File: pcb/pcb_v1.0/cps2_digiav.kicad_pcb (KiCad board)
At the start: 2 copper layers, 93.6 x 46.2 mm, 134 parts, among them J4 HDMI_CONN, P1 JTAG_CONN, U10 S25FL116K, U12 TLV70012, U13 TLV70025, U14 TLV70012, U15 TLV70018, U16 TLV70018, U2 EP4CE15E22, U3 IT6613, U31 74LVC245, U32 74LVC245, U33 74LVC245, U34 SN74LVC3G17, U7 TC1262-3.3VDBTR, U8 TLV70033

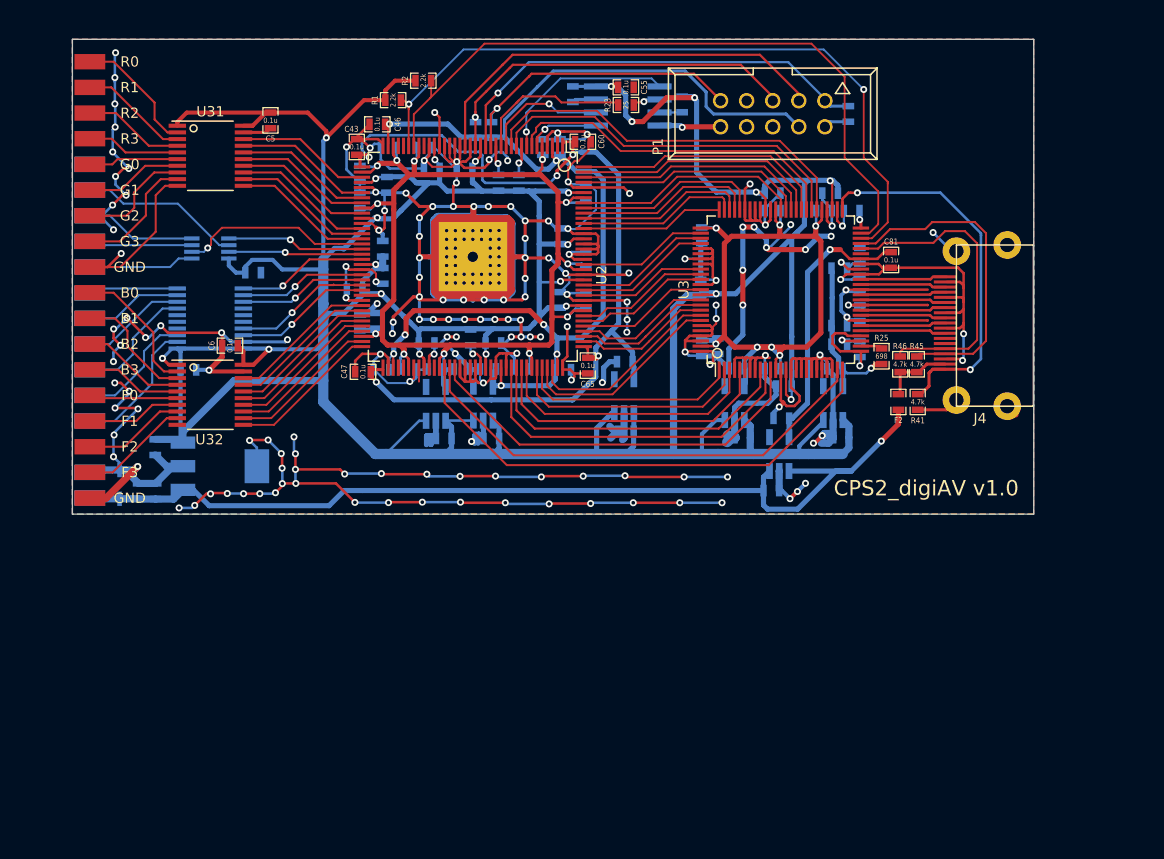
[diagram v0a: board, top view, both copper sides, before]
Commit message: Moved ICs to top, made to fit ontop of CPS2 DIPs
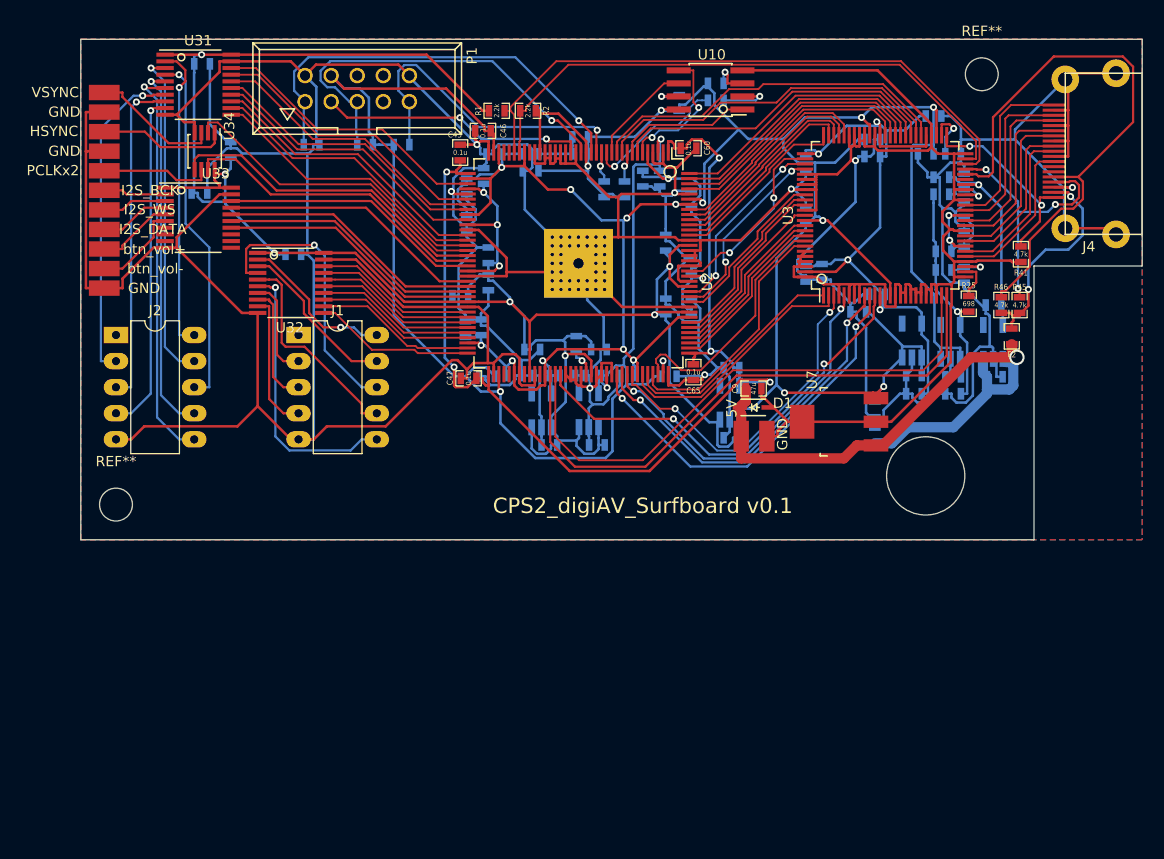
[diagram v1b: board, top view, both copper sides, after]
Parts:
- removed W10: G3, custom_components:SMD_PAD
- removed W11: B0, custom_components:SMD_PAD
- removed W12: B1, custom_components:SMD_PAD
- removed W13: B2, custom_components:SMD_PAD
- removed W14: B3, custom_components:SMD_PAD
- removed W15: F0, custom_components:SMD_PAD
- removed W16: F1, custom_components:SMD_PAD
- removed W17: F2, custom_components:SMD_PAD
- removed W18: F3, custom_components:SMD_PAD
- removed W27, W28: GND, custom_components:SMD_PAD
- removed W3: R0, custom_components:SMD_PAD
- removed W4: R1, custom_components:SMD_PAD
- removed W5: R2, custom_components:SMD_PAD
- removed W6: R3, custom_components:SMD_PAD
- removed W7: G0, custom_components:SMD_PAD
- removed W8: G1, custom_components:SMD_PAD
- removed W9: G2, custom_components:SMD_PAD
- added J1: Conn_02x05, Housings_DIP:DIP-10_W7.62mm_LongPads, F.Cu at (60.3, 52.3)
- added J2: Conn_02x05, Housings_DIP:DIP-10_W7.62mm_LongPads, F.Cu at (42.5, 52.3)
- added REF**: MountingHole_3.2mm_M3, Mounting_Holes:MountingHole_3.2mm_M3, F.Cu at (126.9, 26.9)
- added REF**: MountingHole_3.2mm_M3, Mounting_Holes:MountingHole_3.2mm_M3, F.Cu at (42.5, 68.8)
- C5, C55, C6, C81, R23: moved to B.Cu
- C9, D1, U10, U33, U34, U7, W1, W19, W2, W20, W21, W22, W23, W24, W25, W26, W29, W30, W31: moved to F.Cu
- moved C1 70.3 mm to (116.5, 62.1)
- moved C3 70.2 mm to (116.5, 59.6)
- moved W31 66.0 mm to (105.9, 62.2), turned to 90 degrees
- moved W1 63.7 mm to (103.4, 62.2), turned to 90 degrees
- moved D1 62.3 mm to (104.7, 59.4), turned to 0 degrees
- moved C9 60.7 mm to (104.6, 57.5), turned to 0 degrees
- moved U7 60.5 mm to (113.0, 60.8)
- moved R20 52.4 mm to (61.6, 33.8), turned to 180 degrees
- moved P1 40.5 mm to (66.0, 28.3), turned to 0 degrees
- moved C2 24.4 mm to (128.1, 56.4)
- moved U8 23.5 mm to (128.0, 53.0)
- moved C4 23.4 mm to (128.0, 49.4)
- moved J4 19.8 mm to (135.0, 34.7)
- moved U15 18.3 mm to (120.1, 52.9)
- moved C87 17.8 mm to (120.3, 56.3)
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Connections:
- U33 pad 11: /fpga1/I2S_BCK -> Net-(U33-Pad11)
- U33 pad 12: /fpga1/I2S_WS -> Net-(U33-Pad12)
- U33 pad 13: /fpga1/I2S_DATA -> Net-(U33-Pad13)
- U33 pad 14: Net-(U33-Pad14) -> /fpga1/btn_vol-
- U33 pad 15: Net-(U33-Pad15) -> /fpga1/btn_vol+
- U33 pad 16: Net-(U33-Pad16) -> /fpga1/I2S_DATA
- U33 pad 17: /fpga1/btn_vol+ -> /fpga1/I2S_WS
- U33 pad 18: /fpga1/btn_vol- -> /fpga1/I2S_BCK
- W19 pad 1: Net-(U33-Pad3) -> Net-(U33-Pad5)
- W20 pad 1: Net-(U33-Pad9) -> Net-(U33-Pad2)
- W22 pad 1: Net-(U33-Pad8) -> Net-(U33-Pad3)
- W23 pad 1: Net-(U33-Pad2) -> Net-(U33-Pad6)
- W25 pad 1: Net-(U33-Pad7) -> Net-(U33-Pad4)
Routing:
- net GND: track 885.6 -> 850.0 mm, vias 171 -> 8
- net /5V: track 95.5 -> 62.9 mm
- net Net-(J2-Pad6): track 8.73 -> 39.3 mm, vias 0 -> 1
- net Net-(J2-Pad7): track 9.07 -> 36.3 mm, vias 0 -> 1
- net /hdmitx1/DDC_SCL: track 30.4 -> 56.2 mm
- net /IOVDD: track 450.2 -> 425.4 mm, vias 22 -> 18
- net Net-(J2-Pad8): track 9.84 -> 34.5 mm, vias 0 -> 1
- net Net-(J2-Pad2): track 9.50 -> 31.8 mm, vias 0 -> 1
- net Net-(J2-Pad9): track 10.6 -> 32.5 mm, vias 0 -> 1
- net Net-(J2-Pad3): track 11.1 -> 32.3 mm, vias 0 -> 1
- net Net-(J2-Pad4): track 12.3 -> 33.2 mm, vias 0 -> 1
- net Net-(J1-Pad6): track 8.62 -> 27.2 mm, vias 0 -> 1
- net /fpga1/VSYNC_in: track 13.4 -> 31.8 mm, vias 1 -> 0
- net Net-(J2-Pad10): track 12.3 -> 29.9 mm, vias 0 -> 1
- net /fpga1/HSYNC_in: track 13.1 -> 30.4 mm, vias 1 -> 0
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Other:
- board size 93.6 x 46.2 mm -> 103.4 x 48.7 mm
- board text added: "CPS2_digiAV_Surfboard v0.1"
- board text removed: "CPS2_digiAV v1.0"

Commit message: Added ADV7513
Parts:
- added U1: ADV7513, Housings_QFP:LQFP-64_10x10mm_Pitch0.5mm, F.Cu at (90.8, 82.3)
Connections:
- J4 pad 1: /hdmitx1/TMDS_D2+ -> /hdmitx1/TX2+
- J4 pad 10: /hdmitx1/TMDS_CLK+ -> /hdmitx1/TXC+
- J4 pad 12: /hdmitx1/TMDS_CLK- -> /hdmitx1/TXC-
- J4 pad 15: /hdmitx1/DDC_SCL -> /hdmitx1/DDCSCL
- J4 pad 16: /hdmitx1/DDC_SDA -> /hdmitx1/DDCSDA
- J4 pad 3: /hdmitx1/TMDS_D2- -> /hdmitx1/TX2-
- J4 pad 4: /hdmitx1/TMDS_D1+ -> /hdmitx1/TX1+
- J4 pad 6: /hdmitx1/TMDS_D1- -> /hdmitx1/TX1-
- J4 pad 7: /hdmitx1/TMDS_D0+ -> /hdmitx1/TX0+
- J4 pad 9: /hdmitx1/TMDS_D0- -> /hdmitx1/TX0-
- R45 pad 2: /hdmitx1/DDC_SDA -> /hdmitx1/DDCSDA
- R46 pad 2: /hdmitx1/DDC_SCL -> /hdmitx1/DDCSCL
- U3 pad 1: /hdmitx1/DE -> Net-(U3-Pad1)
- U3 pad 10: /fpga1/HDMITX_I2S_WS -> Net-(U3-Pad10)
- U3 pad 11: /fpga1/HDMITX_I2S_BCK -> Net-(U3-Pad11)
- U3 pad 2: /fpga1/HDMITX_HSYNC -> Net-(U3-Pad2)
- U3 pad 24: /fpga1/HDMITX_INT_N -> Net-(U3-Pad24)
- U3 pad 25: /fpga1/HDMITX_RESET_N -> Net-(U3-Pad25)
- U3 pad 3: /fpga1/HDMITX_VSYNC -> Net-(U3-Pad3)
- U3 pad 48: /fpga1/SCL -> Net-(U3-Pad48)
- U3 pad 49: /fpga1/SDA -> Net-(U3-Pad49)
- U3 pad 5: /fpga1/AUD_MCLK -> Net-(U3-Pad5)
- U3 pad 56: /fpga1/HDMITX_R7 -> Net-(U3-Pad56)
- U3 pad 57: /fpga1/HDMITX_R6 -> Net-(U3-Pad57)
- U3 pad 58: /fpga1/HDMITX_R5 -> Net-(U3-Pad58)
- U3 pad 59: /fpga1/HDMITX_R4 -> Net-(U3-Pad59)
- U3 pad 60: /fpga1/HDMITX_R3 -> Net-(U3-Pad60)
- U3 pad 61: /fpga1/HDMITX_R2 -> Net-(U3-Pad61)
- U3 pad 62: /fpga1/HDMITX_R1 -> Net-(U3-Pad62)
- U3 pad 63: /fpga1/HDMITX_R0 -> Net-(U3-Pad63)
- U3 pad 71: /hdmitx1/G7 -> Net-(U3-Pad71)
- U3 pad 72: /hdmitx1/G6 -> Net-(U3-Pad72)
- U3 pad 73: /hdmitx1/G5 -> Net-(U3-Pad73)
- U3 pad 74: /hdmitx1/G4 -> Net-(U3-Pad74)
- U3 pad 75: /hdmitx1/G3 -> Net-(U3-Pad75)
- U3 pad 77: /hdmitx1/G2 -> Net-(U3-Pad77)
- U3 pad 78: /hdmitx1/G1 -> Net-(U3-Pad78)
- U3 pad 79: /hdmitx1/G0 -> Net-(U3-Pad79)
- U3 pad 84: /hdmitx1/B7 -> Net-(U3-Pad84)
- U3 pad 85: /hdmitx1/B6 -> Net-(U3-Pad85)
- U3 pad 86: /hdmitx1/B5 -> Net-(U3-Pad86)
- U3 pad 88: /fpga1/HDMITX_PCLK -> Net-(U3-Pad88)
- U3 pad 9: /fpga1/HDMITX_I2S_DATA -> Net-(U3-Pad9)
- U3 pad 90: /hdmitx1/B4 -> Net-(U3-Pad90)
- U3 pad 91: /hdmitx1/B3 -> Net-(U3-Pad91)
- U3 pad 92: /hdmitx1/B2 -> Net-(U3-Pad92)
- U3 pad 93: /hdmitx1/B1 -> Net-(U3-Pad93)
- U3 pad 94: /hdmitx1/B0 -> Net-(U3-Pad94)
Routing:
- net /hdmitx1/DDC_SCL: track 56.2 -> 1.09 mm
- net /hdmitx1/DDCSCL: track 0.00 -> 55.2 mm
- net Net-(U3-Pad49): track 0.00 -> 51.8 mm
- net /fpga1/SDA: track 56.4 -> 4.66 mm
- net Net-(U3-Pad25): track 0.00 -> 50.0 mm
- net /fpga1/HDMITX_RESET_N: track 56.6 -> 6.60 mm
- net Net-(U3-Pad9): track 0.00 -> 25.3 mm, vias 0 -> 1
- net /fpga1/HDMITX_I2S_DATA: track 37.5 -> 12.2 mm, vias 2 -> 1
- net /hdmitx1/DDC_SDA: track 26.2 -> 2.04 mm, vias 3 -> 1
- net /hdmitx1/DDCSDA: track 0.00 -> 24.2 mm, vias 0 -> 2
- net Net-(U3-Pad93): track 0.00 -> 23.2 mm
- net /hdmitx1/B1: track 24.1 -> 0.92 mm
- net Net-(U3-Pad94): track 0.00 -> 22.9 mm
- net /hdmitx1/B0: track 24.6 -> 1.67 mm
- net /fpga1/HDMITX_I2S_WS: track 39.1 -> 17.5 mm, vias 2 -> 1
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
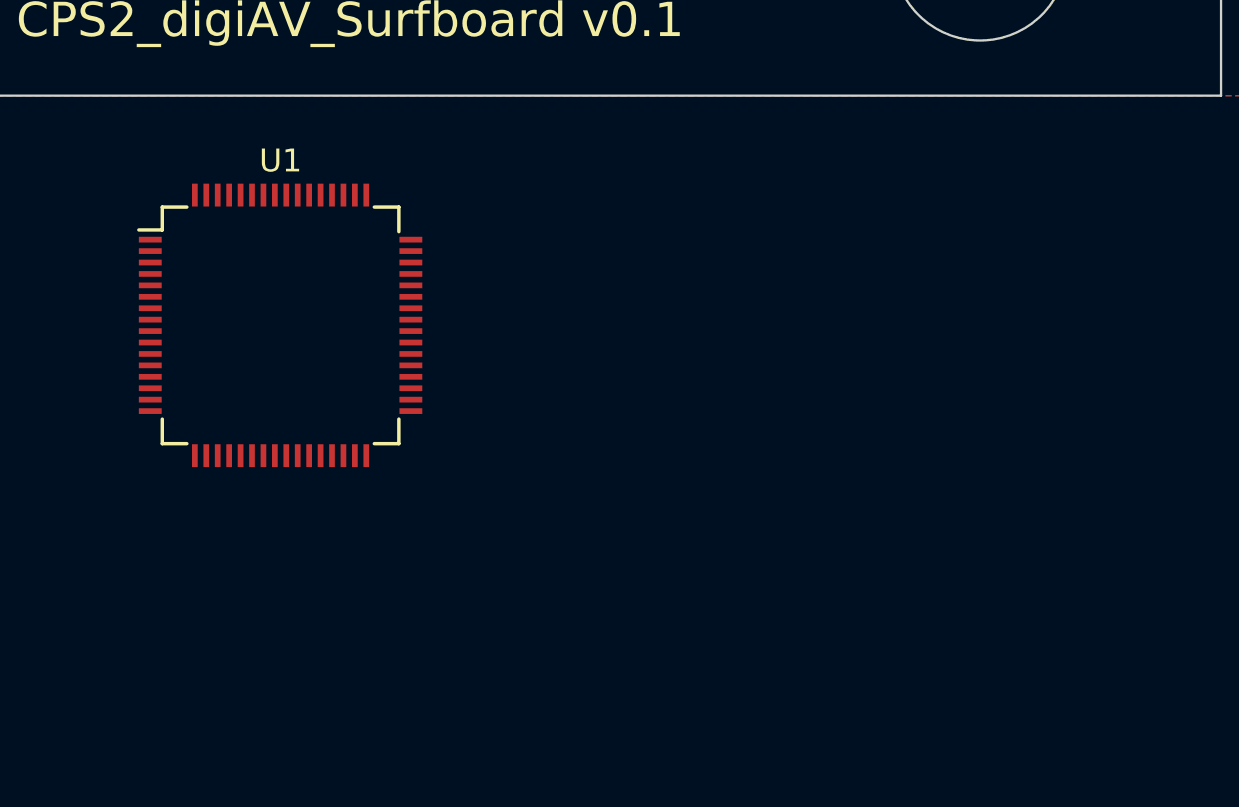
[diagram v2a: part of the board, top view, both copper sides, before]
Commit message: Finished power section of ADV7531
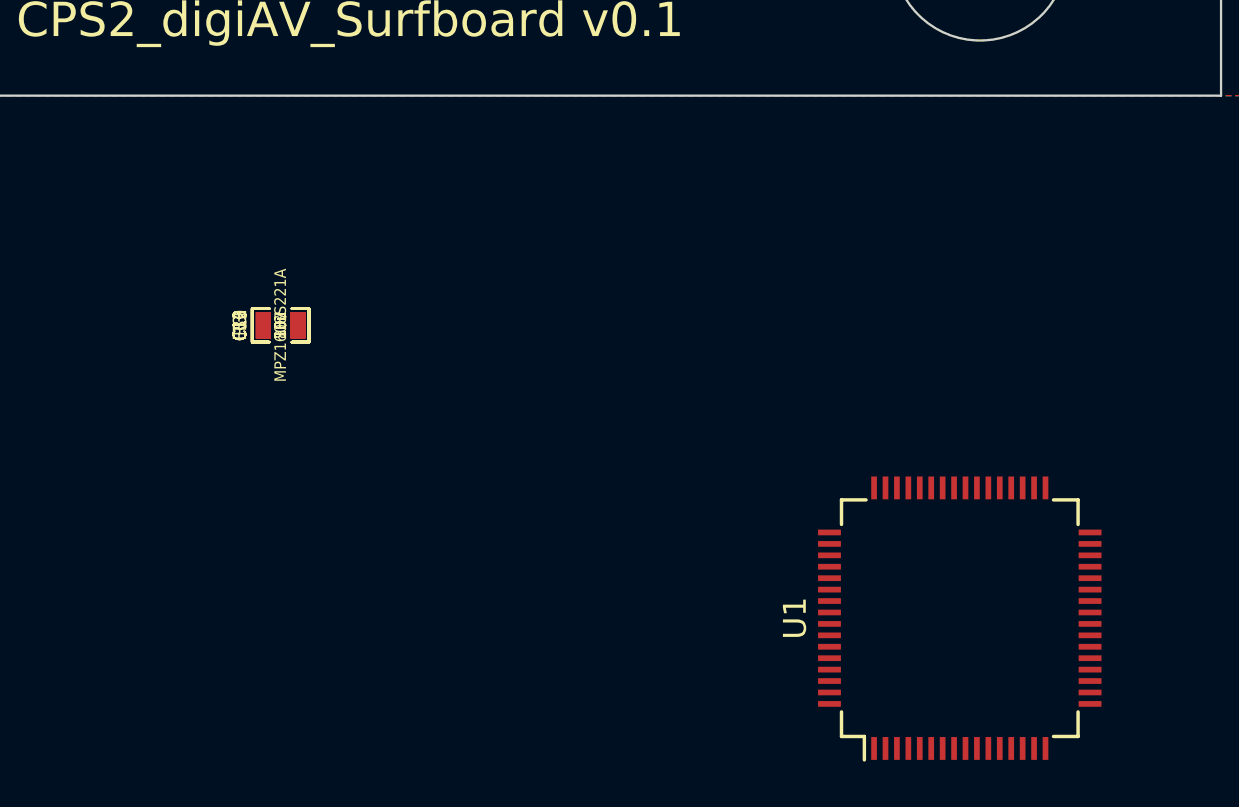
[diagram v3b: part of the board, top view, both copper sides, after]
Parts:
- added C10, C11, C12, C13: 10u, custom_components:SM0603_Capa_libcms, F.Cu at (90.8, 82.3)
- added FB3: MPZ1608S221A, custom_components:SM0603_Resistor_libcms, F.Cu at (90.8, 82.3)
- added R3: 887, custom_components:SM0603_Resistor_libcms, F.Cu at (90.8, 82.3)
- moved U1 32.4 mm to (120.5, 95.1), turned to 90 degrees
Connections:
- C110 pad 1: /hdmitx1/DVDD1V8 -> /hdmitx1/AVDD1V8
- C69 pad 1: /hdmitx1/DVDD1V8 -> Net-(C12-Pad1)
- C73 pad 1: /IOVDD -> Net-(C12-Pad1)
- C74 pad 1: Net-(C74-Pad1) -> /hdmitx1/AVDD1V8
- C75 pad 1: /hdmitx1/DVDD1V8 -> /IOVDD
- C77 pad 1: Net-(C77-Pad1) -> Net-(C10-Pad1)
- C78 pad 1: Net-(C77-Pad1) -> Net-(C10-Pad1)
- C79 pad 1: /IOVDD -> Net-(C13-Pad1)
- C80 pad 1: Net-(C80-Pad1) -> Net-(C10-Pad1)
- C81 pad 1: /A33VDD -> Net-(C10-Pad1)
- C82 pad 1: /hdmitx1/DVDD1V8 -> Net-(C11-Pad1)
- C83 pad 1: /IOVDD -> Net-(C13-Pad1)
- C84 pad 1: /hdmitx1/DVDD1V8 -> Net-(C13-Pad1)
- C85 pad 1: /hdmitx1/DVDD1V8 -> /hdmitx1/AVDD1V8
- C86 pad 1: /IOVDD -> /hdmitx1/PVDD1V8
- C87 pad 1: /IOVDD -> /A33VDD
- C88 pad 1: /IOVDD -> /A33VDD
- C89 pad 1: /hdmitx1/DVDD1V8 -> /hdmitx1/AVDD1V8
- C90 pad 1: /hdmitx1/AVCC1V8 -> /hdmitx1/PVDD1V8
- FB1 pad 1: /hdmitx1/AVCC1V8 -> Net-(C13-Pad1)
- FB1 pad 2: Net-(C74-Pad1) -> /hdmitx1/AVDD1V8
- FB2 pad 1: /hdmitx1/AVCC1V8 -> Net-(C12-Pad1)
- FB2 pad 2: Net-(C77-Pad1) -> /hdmitx1/PVDD1V8
- FB4 pad 1: /hdmitx1/AVCC1V8 -> /IOVDD
- FB4 pad 2: Net-(C80-Pad1) -> Net-(C11-Pad1)
- U1 pad 1: Net-(U1-Pad1) -> Net-(C10-Pad1)
- U1 pad 11: Net-(U1-Pad11) -> Net-(C10-Pad1)
- U1 pad 12: Net-(U1-Pad12) -> Net-(C12-Pad1)
- U1 pad 13: Net-(U1-Pad13) -> Net-(C12-Pad1)
- U1 pad 15: Net-(U1-Pad15) -> Net-(C13-Pad1)
- U1 pad 19: Net-(U1-Pad19) -> Net-(C13-Pad1)
- U1 pad 25: Net-(U1-Pad25) -> Net-(C13-Pad1)
- U1 pad 29: Net-(U1-Pad29) -> Net-(C11-Pad1)
- U1 pad 31: Net-(U1-Pad31) -> Net-(C10-Pad1)
- U1 pad 51: Net-(U1-Pad51) -> Net-(C10-Pad1)
- U15 pad 1: /IOVDD -> /A33VDD
- U15 pad 3: /IOVDD -> /A33VDD
- U15 pad 5: /hdmitx1/DVDD1V8 -> /hdmitx1/AVDD1V8
- U16 pad 1: /IOVDD -> /A33VDD
- U16 pad 3: /IOVDD -> /A33VDD
- U16 pad 5: /hdmitx1/AVCC1V8 -> /hdmitx1/PVDD1V8
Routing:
- net /IOVDD: track 425.4 -> 359.9 mm, vias 18 -> 17
- net /hdmitx1/PVDD1V8: track 0.00 -> 46.7 mm, vias 0 -> 3
- net /hdmitx1/DVDD1V8: track 68.5 -> 22.4 mm, vias 4 -> 3
- net /fpga1/SDA: track 4.66 -> 43.1 mm
- net Net-(U3-Pad49): track 51.8 -> 13.3 mm
- net Net-(C13-Pad1): track 0.00 -> 29.9 mm
- net Net-(C12-Pad1): track 0.00 -> 24.8 mm, vias 0 -> 1
- net Net-(U3-Pad25): track 50.0 -> 27.1 mm
- net /fpga1/HDMITX_RESET_N: track 6.60 -> 29.4 mm
- net Net-(U3-Pad9): track 25.3 -> 3.45 mm
- net /fpga1/HDMITX_I2S_DATA: track 12.2 -> 34.1 mm
- net /hdmitx1/AVDD1V8: track 0.00 -> 20.3 mm, vias 0 -> 1
- net /fpga1/HDMITX_I2S_WS: track 17.5 -> 37.4 mm, vias 1 -> 2
- net Net-(U3-Pad10): track 21.6 -> 1.70 mm, vias 1 -> 0
- net /hdmitx1/AVCC1V8: track 22.5 -> 4.45 mm
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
